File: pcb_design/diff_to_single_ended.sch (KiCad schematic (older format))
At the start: 9 parts, among them U14 OPA2376AID

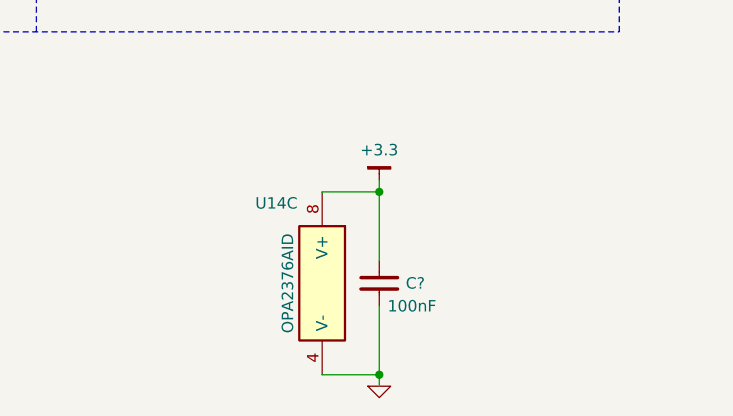
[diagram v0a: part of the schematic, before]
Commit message: Fixed issue with non-bidirectional phase current measurement. Started routing power supplies. Changed terminal blocks from 5.00mm to 3.81mm pitch
Signed-off-by: Marcos Chaparro <mchaparro@paltatech.com>
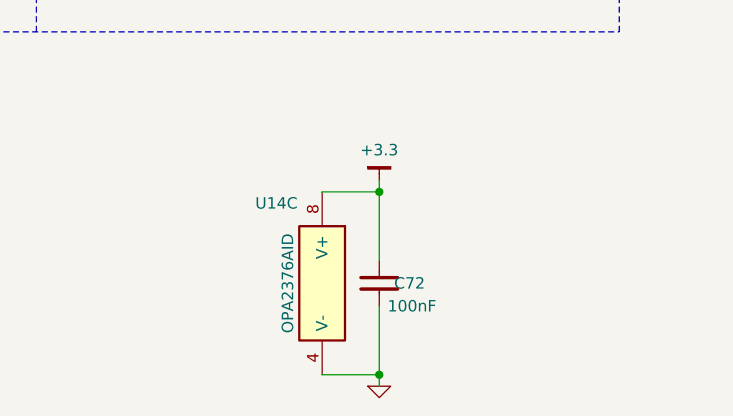
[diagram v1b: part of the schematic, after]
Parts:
- gave numbers to parts that had none: 1
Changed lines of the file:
@@
 encoding utf-8
 Sheet 13 13
-Title ""
-Date ""
-Rev ""
-Comp ""
+Title "Differential to single ended"
+Date "2017-01-24"
+Rev "0.1"
+Comp "vedder.se + PALTA TECH S.A. + PYMCO.fr"
 Comment1 ""
 Comment2 ""
@@
 AR Path="/588C2790/588F226F" Ref="#PWR?"  Part="1"
 AR Path="/588C4E84/588F226F" Ref="#PWR?"  Part="1"
-AR Path="/588DB05E/588F226F" Ref="#PWR154"  Part="1"
-F 0 "#PWR154" H 5950 4550 30  0001 C CNN
+AR Path="/588DB05E/588F226F" Ref="#PWR0159"  Part="1"
+F 0 "#PWR0159" H 5950 4550 30  0001 C CNN
 F 1 "GND" H 5950 4480 30  0001 C CNN
 F 2 "" H 5950 4550 60  0000 C CNN
@@
 AR Path="/588C2790/588F2EA3" Ref="C?"  Part="1"
 AR Path="/588C4E84/588F2EA3" Ref="C?"  Part="1"
-AR Path="/588DB05E/588F2EA3" Ref="C?"  Part="1"
-F 0 "C?" H 6850 5950 50  0000 L CNN
+AR Path="/588DB05E/588F2EA3" Ref="C72"  Part="1"
+F 0 "C72" H 6850 5950 50  0000 L CNN
 F 1 "100nF" H 6800 5850 50  0000 L CNN
 F 2 "IPC7351-Nominal:CAPC1608X55" H 7050 5950 50  0001 C CNN
@@
 	7050 6050 7050 6400
 $Comp
-L GND #PWR?
+L GND #PWR0160
 U 1 1 588F3171
 P 7050 6400
-F 0 "#PWR?" H 7100 6450 30  0001 C CNN
+F 0 "#PWR0160" H 7100 6450 30  0001 C CNN
 F 1 "GND" H 0   780 30  0001 C CNN
 F 2 "" H 0   850 60  0000 C CNN
@@
 Connection ~ 7050 6350
 $Comp
-L +3.3 #PWR?
+L +3.3 #PWR0161
 U 1 1 588F3249
 P 7050 5500
-F 0 "#PWR?" H 7100 5550 30  0001 C CNN
+F 0 "#PWR0161" H 7100 5550 30  0001 C CNN
 F 1 "+3.3" H 7050 5633 50  0000 C CNN
 F 2 "" H -50 0   60  0000 C CNN

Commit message: More layout
Signed-off-by: Marcos Chaparro <mchaparro@paltatech.com>
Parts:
- added R121: 2k, IPC7351-Nominal:RESC1608X50, symbol R-0603
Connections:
- net IN+: now also R121.2
- net IN-: now also R121.1
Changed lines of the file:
@@
 Comment4 ""
 $EndDescr
-Text HLabel 4800 4000 0    60   Input ~ 0
+Text HLabel 4500 4000 0    60   Input ~ 0
 IN+
-Text HLabel 4800 4200 0    60   Input ~ 0
+Text HLabel 4500 4200 0    60   Input ~ 0
 IN-
 Text HLabel 7500 4100 2    60   Output ~ 0
@@
 AR Path="/588C2790/588F226F" Ref="#PWR?"  Part="1"
 AR Path="/588C4E84/588F226F" Ref="#PWR?"  Part="1"
-AR Path="/588DB05E/588F226F" Ref="#PWR0159"  Part="1"
-F 0 "#PWR0159" H 5950 4550 30  0001 C CNN
+AR Path="/588DB05E/588F226F" Ref="#PWR160"  Part="1"
+F 0 "#PWR160" H 5950 4550 30  0001 C CNN
 F 1 "GND" H 5950 4480 30  0001 C CNN
 F 2 "" H 5950 4550 60  0000 C CNN
@@
 1st order filter (TBD)
 Wire Wire Line
-	4800 4000 5000 4000
-Wire Wire Line
-	4800 4200 5000 4200
+	4500 4000 5000 4000
+Wire Wire Line
+	4500 4200 5000 4200
 Wire Notes Line
 	3600 3100 3600 4850
@@
 	7050 6050 7050 6400
 $Comp
-L GND #PWR0160
+L GND #PWR162
 U 1 1 588F3171
 P 7050 6400
-F 0 "#PWR0160" H 7100 6450 30  0001 C CNN
+F 0 "#PWR162" H 7100 6450 30  0001 C CNN
 F 1 "GND" H 0   780 30  0001 C CNN
 F 2 "" H 0   850 60  0000 C CNN
@@
 Connection ~ 7050 6350
 $Comp
-L +3.3 #PWR0161
+L +3.3 #PWR161
 U 1 1 588F3249
 P 7050 5500
-F 0 "#PWR0161" H 7100 5550 30  0001 C CNN
+F 0 "#PWR161" H 7100 5550 30  0001 C CNN
 F 1 "+3.3" H 7050 5633 50  0000 C CNN
 F 2 "" H -50 0   60  0000 C CNN
@@
 $EndComp
 Connection ~ 7050 5550
+$Comp
+L R-0603 R?
+U 1 1 588DF124
+P 4800 4100
+AR Path="/5886DA84/588DF124" Ref="R?"  Part="1"
+AR Path="/588C2790/588DF124" Ref="R?"  Part="1"
+AR Path="/588C4E84/588DF124" Ref="R?"  Part="1"
+AR Path="/588DB05E/588DF124" Ref="R121"  Part="1"
+F 0 "R121" V 4700 4100 50  0000 C CNN
+F 1 "2k" V 4800 4100 30  0000 C CNN
+F 2 "IPC7351-Nominal:RESC1608X50" H 4800 4100 50  0001 C CNN
+F 3 "" H 4800 4150 60  0000 C CNN
+F 4 "RES SMD 1k 5% [0603]" H 5550 4650 60  0001 C CNN "BOM"
+	1    4800 4100
+	-1   0    0    1
+$EndComp
+Connection ~ 4800 4000
+Connection ~ 4800 4200
 $EndSCHEMATC

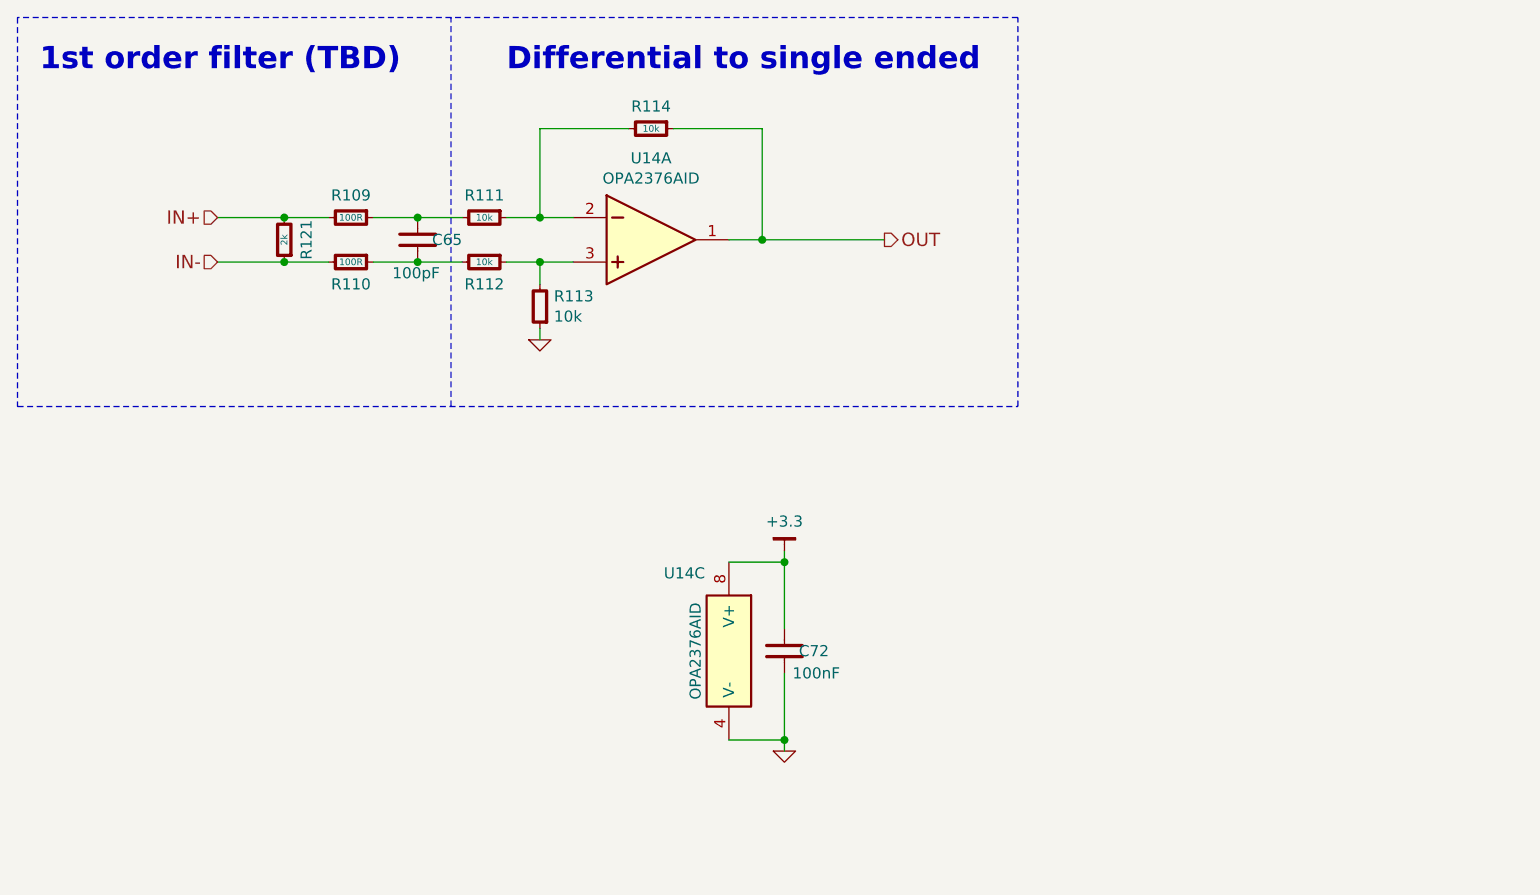
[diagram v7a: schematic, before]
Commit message: Updated component values according to simulations. 1.5khz for user inputs and  240khz lp pass filters for motor control
Signed-off-by: Marcos Chaparro <mchaparro@paltatech.com>
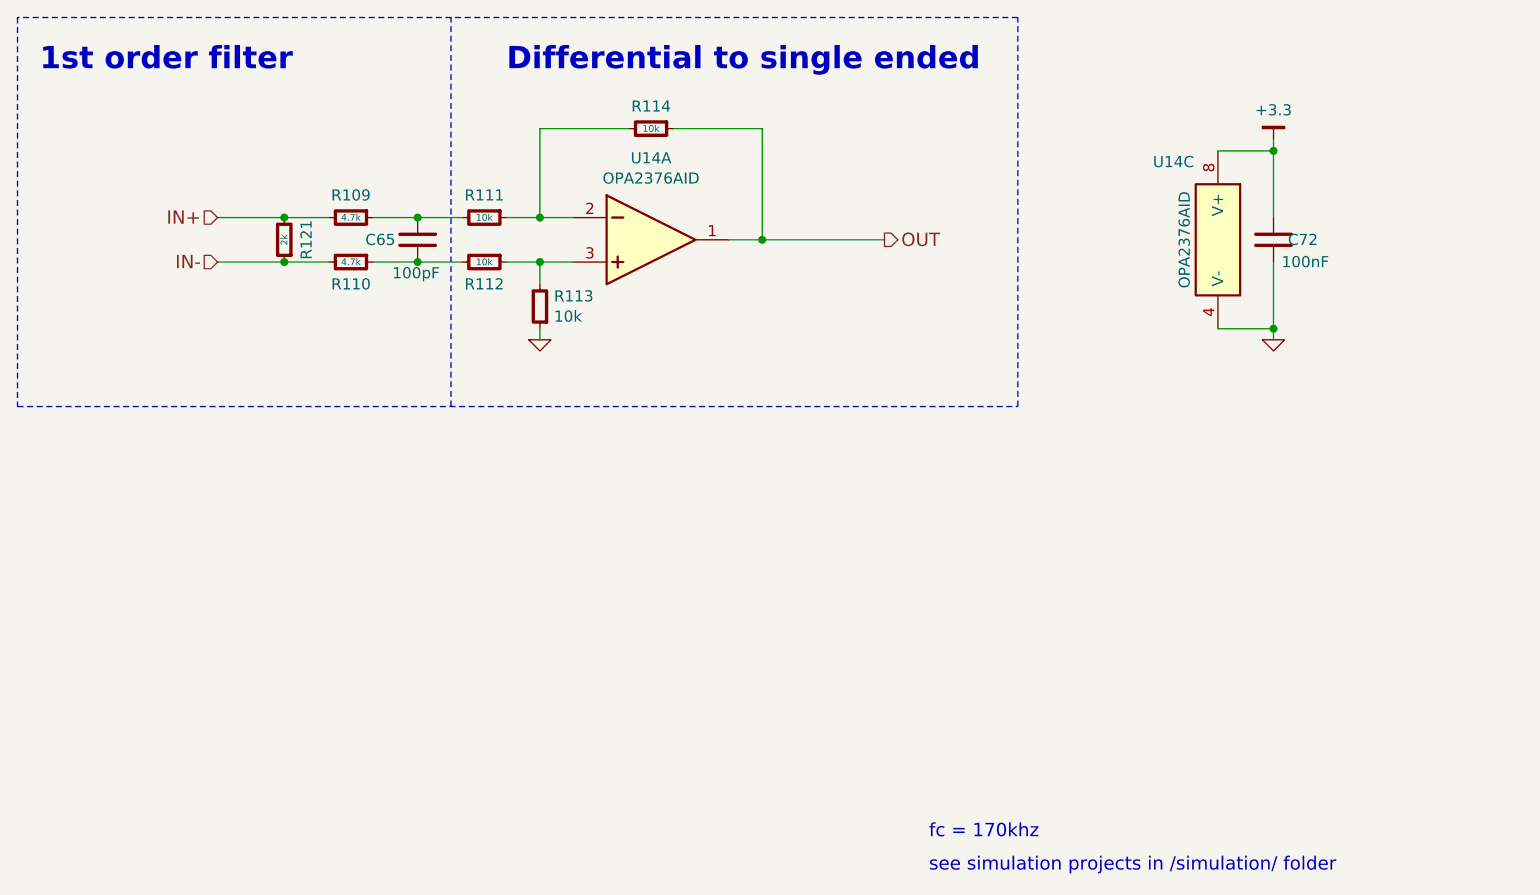
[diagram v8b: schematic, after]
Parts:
- R109, R110: value 100R -> 4.7k
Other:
- note added: "1st order filter"
- note added: "fc = 170khz"
- note added: "see simulation projects in /simulation/ folder"
- note removed: "1st order filter (TBD)"
- moved on the sheet: C72, U14C
